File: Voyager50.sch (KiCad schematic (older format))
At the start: 193 parts, among them Q1 2N7002, SW1 SW_Push, U1 ATmega32U2-MU, U2 PRTR5V0U2X, Y1 16Mhz

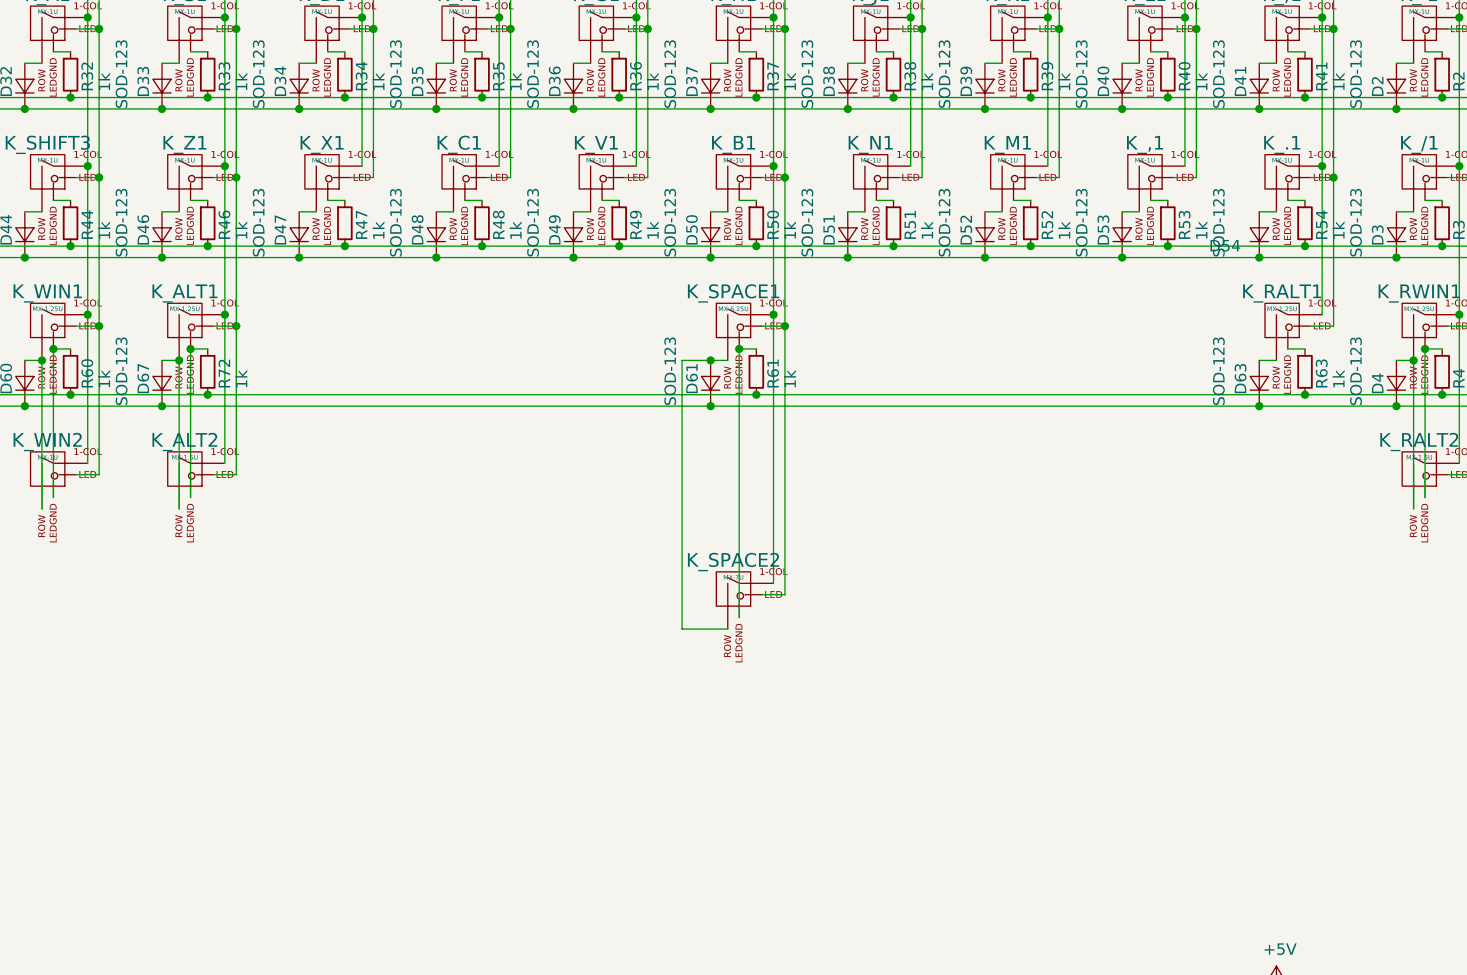
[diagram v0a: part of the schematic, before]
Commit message: Add split space
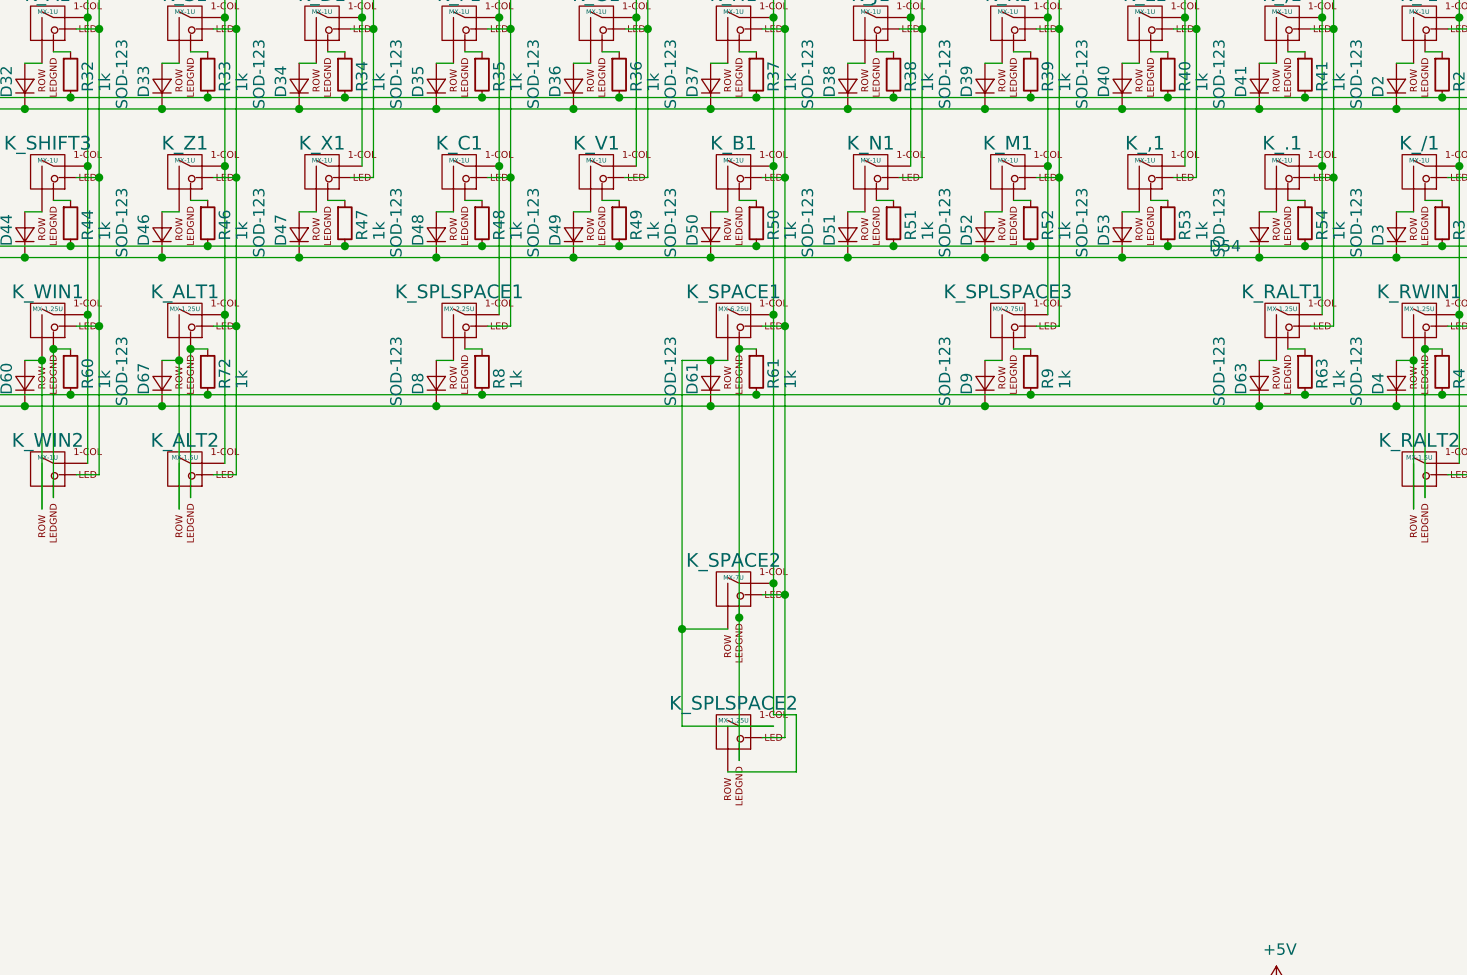
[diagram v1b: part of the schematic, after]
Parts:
- added D8, D9: SOD-123, Diodes_SMD:D_SOD-123, symbol Device:D_Small
- added K_SPLSPACE1: MX-2.25U, MX_Alps_Hybrid:MX-2.25U-ReversedStabilizers, symbol MX_Alps_Hybrids:MX-1U
- added K_SPLSPACE2: MX-1.25U, MX_Alps_Hybrid:MX-1.25U-FLIPPED, symbol MX_Alps_Hybrids:MX-1U
- added K_SPLSPACE3: MX-2.75U, MX_Alps_Hybrid:MX-2.75U-ReversedStabilizers, symbol MX_Alps_Hybrids:MX-1U
- added R8, R9: 1k, Resistors_SMD:R_0603, symbol Device:R_Small
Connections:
- net +5V: now also K_SPLSPACE1.3 (LED), K_SPLSPACE2.3 (LED), K_SPLSPACE3.3 (LED)
- net COL4: now also K_SPLSPACE1.1 (COL)
- net COL6: now also K_SPLSPACE2.2 (ROW)
- net COL8: now also K_SPLSPACE3.1 (COL)
- net LEDGND: now also R8.2, R9.2
- net ROW3: now also D8.1 (K), D9.1 (K)
- net at D61.2 (A), K_SPACE1.2 (ROW), K_SPACE2.2 (ROW): now also K_SPLSPACE2.1 (COL)
- net at K_SPACE1.4 (LEDGND), K_SPACE2.4 (LEDGND), R61.1: now also K_SPLSPACE2.4 (LEDGND)
- new net: D8.2 (A), K_SPLSPACE1.2 (ROW)
- new net: K_SPLSPACE1.4 (LEDGND), R8.1
- new net: D9.2 (A), K_SPLSPACE3.2 (ROW)
- new net: K_SPLSPACE3.4 (LEDGND), R9.1
